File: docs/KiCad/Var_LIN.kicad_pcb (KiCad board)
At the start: 2 copper layers, 39 x 22.4 mm, 27 parts, among them J2 Conn_01x04_Pin, J3 Conn_01x04_Pin, U4 TGS_2611-E00, U5 TLIN2029ADRBRQ1, U6 LMR50410, U7 ATtiny412-SS, U8 BTS4142N

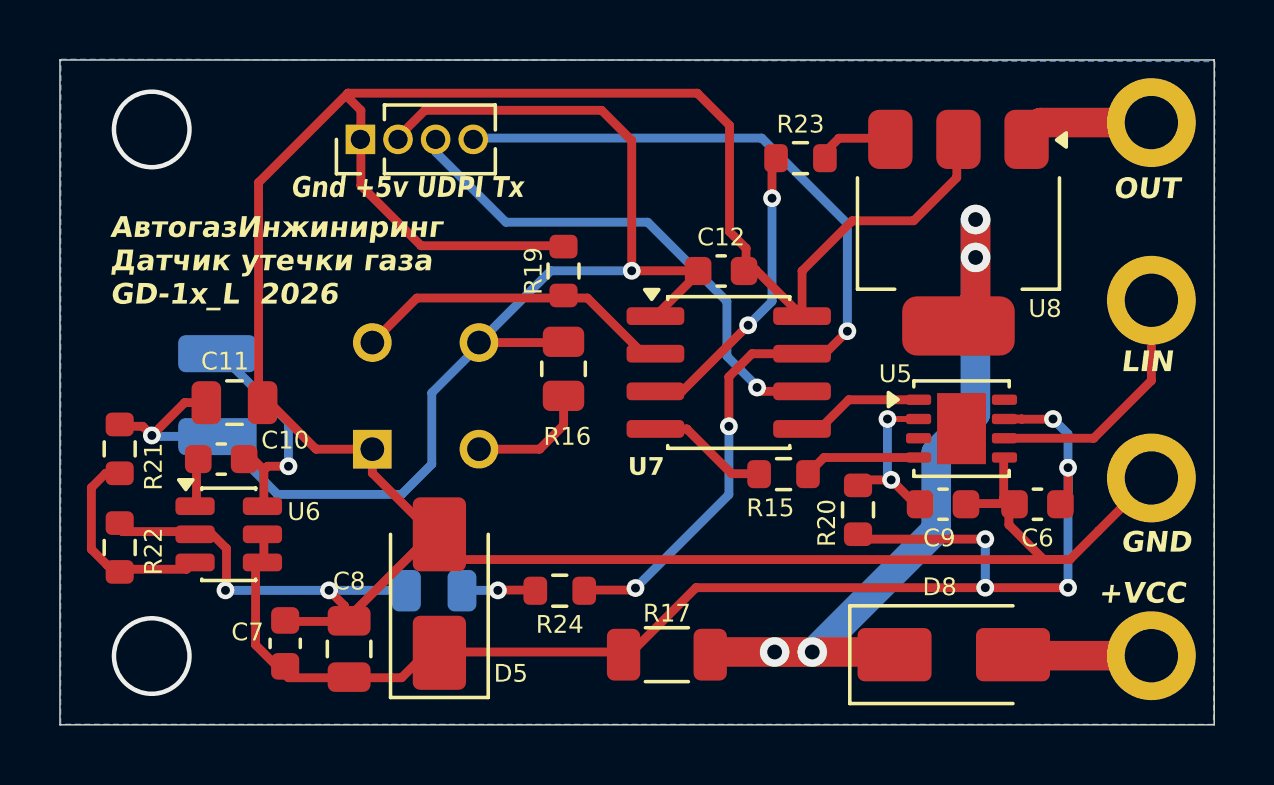
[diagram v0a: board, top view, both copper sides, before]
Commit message: Изменить выходной ключ на умный. Правки печатной платы
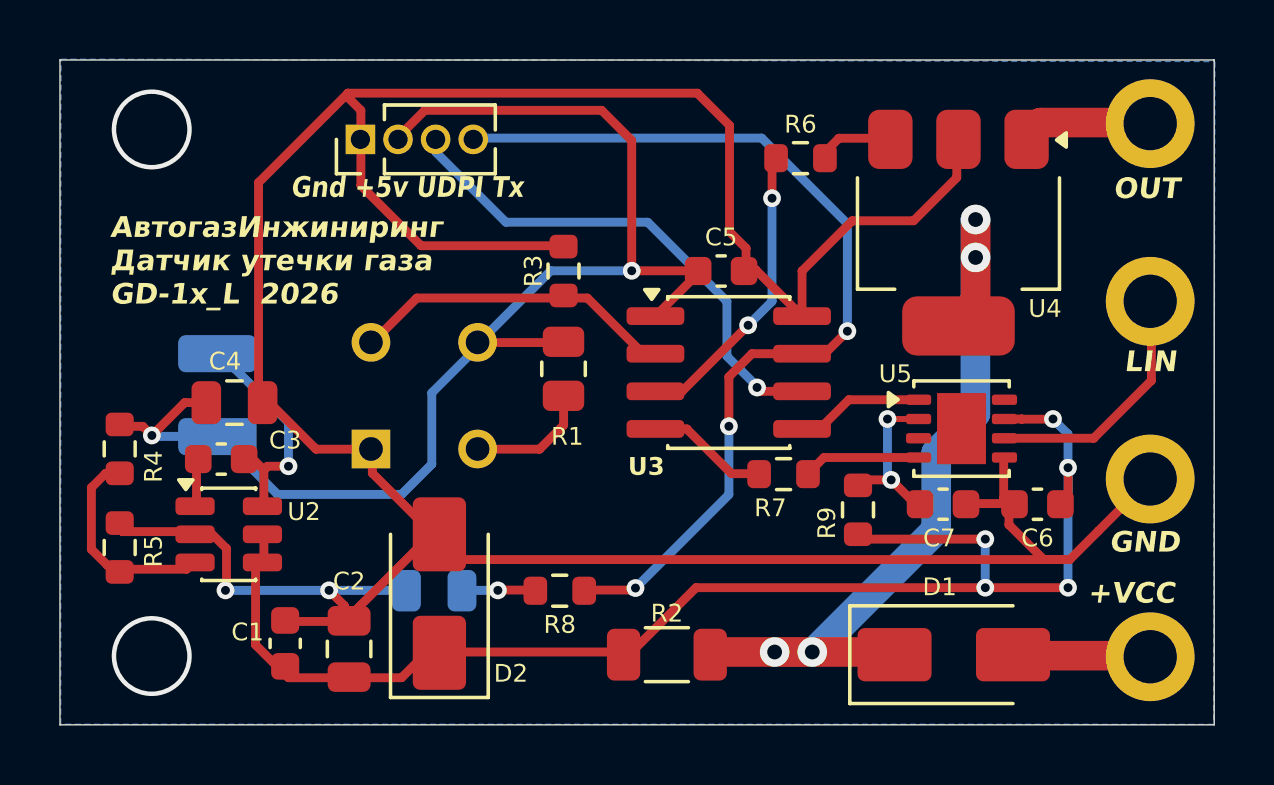
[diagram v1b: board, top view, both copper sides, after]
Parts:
- removed the U4 at (124.9, 103.7)
- added U1: TGS_2611-E00, Sensor_Humidity:TO180P920X780-4P, B.Cu at (124.8, 103.7)
- J2: footprint Connector_Pin:AMP SEAL 3.00mm_4p -> Connector_DIN:SSEAL_4
- moved J2 12.9 mm to (143.0, 101.2), turned to 0 degrees
- renumbered C7 to C1, C8 to C2, C10 to C3, C11 to C4, C12 to C5, C9 to C7, D8 to D1, D5 to D2, D6 to D3, J3 to J1, L2 to L1, R16 to R1, R17 to R2, R19 to R3, R21 to R4, R22 to R5, R23 to R6, R15 to R7, R24 to R8, R20 to R9, U6 to U2, U7 to U3, U8 to U4

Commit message: Коррекция ПП. Замена выходной ключ на BTS72002
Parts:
- R2: footprint Resistor_SMD:R_1206_3216Metric -> Resistor_SMD:R_0805_2012Metric
- U1: value TGS_2611-E00 -> TGS_2611-E
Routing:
- net GND: track 112.6 -> 112.0 mm

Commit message: Обновить схемы и логику выходного ключа
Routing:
- net Net-(D2-A1): track 48.4 -> 44.9 mm, vias 5 -> 4
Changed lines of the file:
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@@
+	)
+	(segment
+		(start 119.4235 109.173)
+		(end 119.4235 108.223)
+		(width 0.3)
+		(layer "F.Cu")
+		(net "Net-(D2-A1)")
+	)
+	(segment
+		(start 146.0665 104.438)
+		(end 146.0615 104.443)
+		(width 0.3)
+		(layer "F.Cu")
+		(net "Net-(D2-A1)")
+	)
+	(segment
+		(start 143.1 110.133)
+		(end 134.013557 110.133)
+		(width 0.3)
+		(layer "F.Cu")
+		(net "Net-(D2-A1)")
+	)
+	(segment
+		(start 146.0615 104.443)
+		(end 145.0135 104.443)
+		(width 0.3)
+		(layer "F.Cu")
+		(net "Net-(D2-A1)")
+	)
+	(segment
+		(start 134.013557 110.133)
+		(end 131.8425 112.304057)
+		(width 0.3)
+		(layer "F.Cu")
+		(net "Net-(D2-A1)")
+	)
+	(segment
+		(start 124.0735 113.173)
+		(end 120.250471 113.173)
+		(width 0.3)
+		(layer "F.Cu")
+		(net "Net-(D2-A1)")
 	)
 	(segment
@@
 	)
 	(segment
-		(start 122.1435 113.173)
+		(start 145.0135 104.443)
+		(end 145.0085 104.438)
+		(width 0.3)
+		(layer "F.Cu")
+		(net "Net-(D2-A1)")
+	)
+	(segment
+		(start 125.124557 112.304057)
+		(end 125.0335 112.213)
+		(width 0.3)
+		(layer "F.Cu")
+		(net "Net-(D2-A1)")
+	)
+	(segment
+		(start 146.5745 107.171943)
+		(end 146.453443 107.293)
+		(width 0.3)
+		(layer "F.Cu")
+		(net "Net-(D2-A1)")
+	)
+	(segment
+		(start 131.8425 112.304057)
+		(end 125.124557 112.304057)
+		(width 0.3)
+		(layer "F.Cu")
+		(net "Net-(D2-A1)")
+	)
+	(segment
+		(start 125.0335 112.213)
 		(end 124.0735 113.173)
 		(width 0.3)
@@
 	)
 	(segment
-		(start 134.013557 110.133)
-		(end 131.8425 112.304057)
-		(width 0.3)
-		(layer "F.Cu")
-		(net "Net-(D2-A1)")
-	)
-	(segment
-		(start 146.0665 104.438)
-		(end 146.0615 104.443)
+		(start 146.5745 106.081057)
+		(end 146.5745 107.171943)
+		(width 0.3)
+		(layer "F.Cu")
+		(net "Net-(D2-A1)")
+	)
+	(segment
+		(start 143.7805 108.494057)
+		(end 139.739557 108.494057)
 		(width 0.3)
 		(layer "F.Cu")
@@
 	)
 	(segment
-		(start 146.0615 104.443)
-		(end 145.0135 104.443)
-		(width 0.3)
-		(layer "F.Cu")
-		(net "Net-(D2-A1)")
-	)
-	(segment
-		(start 131.8425 112.304057)
-		(end 125.124557 112.304057)
-		(width 0.3)
-		(layer "F.Cu")
-		(net "Net-(D2-A1)")
-	)
-	(segment
-		(start 124.0735 113.173)
-		(end 125.0335 112.213)
-		(width 0.3)
-		(layer "F.Cu")
-		(net "Net-(D2-A1)")
-	)
-	(segment
-		(start 125.124557 112.304057)
-		(end 125.0335 112.213)
-		(width 0.3)
-		(layer "F.Cu")
-		(net "Net-(D2-A1)")
-	)
-	(segment
-		(start 143.7805 110.133)
-		(end 134.013557 110.133)
-		(width 0.3)
-		(layer "F.Cu")
-		(net "Net-(D2-A1)")
-	)
-	(segment
-		(start 146.5745 110.133)
-		(end 143.7805 110.133)
-		(width 0.3)
-		(layer "F.Cu")
-		(net "Net-(D2-A1)")
-	)
-	(segment
-		(start 145.0135 104.443)
-		(end 145.0085 104.438)
-		(width 0.3)
-		(layer "F.Cu")
-		(net "Net-(D2-A1)")
-	)
-	(segment
-		(start 146.5745 107.171943)
-		(end 146.453443 107.293)
-		(width 0.3)
-		(layer "F.Cu")
-		(net "Net-(D2-A1)")
-	)
-	(segment
-		(start 146.5745 106.081057)
-		(end 146.5745 107.171943)
-		(width 0.3)
-		(layer "F.Cu")
-		(net "Net-(D2-A1)")
-	)
-	(segment
-		(start 143.7805 108.494057)
-		(end 139.739557 108.494057)
-		(width 0.3)
-		(layer "F.Cu")
-		(net "Net-(D2-A1)")
-	)
-	(segment
-		(start 122.1435 113.173)
-		(end 120.250471 113.173)
+		(start 145.0085 104.438)
+		(end 144.401 104.438)
+		(width 0.3)
+		(layer "F.Cu")
+		(net "Net-(D2-A1)")
+	)
+	(segment
+		(start 146.453443 107.293)
+		(end 146.1285 107.293)
+		(width 0.3)
+		(layer "F.Cu")
+		(net "Net-(D2-A1)")
+	)
+	(segment
+		(start 139.739557 108.494057)
+		(end 139.4935 108.248)
 		(width 0.3)
 		(layer "F.Cu")
@@
 		(net "Net-(D2-A1)")
 	)
-	(segment
-		(start 119.4235 109.173)
-		(end 119.4235 108.223)
-		(width 0.3)
-		(layer "F.Cu")
-		(net "Net-(D2-A1)")
-	)
-	(segment
-		(start 145.0085 104.438)
-		(end 144.401 104.438)
-		(width 0.3)
-		(layer "F.Cu")
-		(net "Net-(D2-A1)")
-	)
-	(segment
-		(start 146.453443 107.293)
-		(end 146.1285 107.293)
-		(width 0.3)
-		(layer "F.Cu")
-		(net "Net-(D2-A1)")
-	)
-	(segment
-		(start 139.739557 108.494057)
-		(end 139.4935 108.248)
-		(width 0.3)
-		(layer "F.Cu")
-		(net "Net-(D2-A1)")
-	)
 	(via
 		(at 146.0665 104.438)
@@
 	)
 	(via
-		(at 146.5745 110.133)
-		(size 0.6)
-		(drill 0.3)
-		(layers "F.Cu" "B.Cu")
-		(net "Net-(D2-A1)")
-	)
-	(via
 		(at 146.5745 106.081057)
 		(size 0.6)
@@
 	)
 	(via
-		(at 143.7805 110.133)
-		(size 0.6)
-		(drill 0.3)
-		(layers "F.Cu" "B.Cu")
-		(net "Net-(D2-A1)")
-	)
-	(segment
-		(start 143.7805 110.133)
+		(at 143.1 110.133)
+		(size 0.6)
+		(drill 0.3)
+		(layers "F.Cu" "B.Cu")
+		(net "Net-(D2-A1)")
+	)
+	(segment
+		(start 143.7805 109.4525)
 		(end 143.7805 108.494057)
 		(width 0.3)
@@
 	)
 	(segment
-		(start 146.5745 110.133)
-		(end 146.5745 106.081057)
+		(start 143.1 110.133)
+		(end 143.7805 109.4525)
 		(width 0.3)
 		(layer "B.Cu")
@@
 	)
 	(segment
+		(start 143.7805 108.494057)
+		(end 144.1615 108.494057)
+		(width 0.3)
+		(layer "B.Cu")
+		(net "Net-(D2-A1)")
+	)
+	(segment
 		(start 146.5745 106.081057)
 		(end 146.5745 104.946)
 		(width 0.3)
 		(layer "B.Cu")
+		(net "Net-(D2-A1)")
+	)
+	(segment
+		(start 144.1615 108.494057)
+		(end 146.5745 106.081057)
+		(width 0.3)
+		(layer "B.Cu")
